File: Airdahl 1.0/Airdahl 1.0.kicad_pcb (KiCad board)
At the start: 2 copper layers, 60.5 x 38 mm, 94 parts, among them J1 Conn_01x04, J2 DF40C-34DS-0.4V_58_, J3 DF40C-34DS-0.4V_58_, J4 USB_C_Receptacle_USB2.0_16P, J7 CONUFL001-SMD-T, J9 104031-0811, SW1 SW_MEC_5E, SW2 SW_MEC_5E, U1 STM32F446RETx, U2 MCP2200-I-MQ, U4 BNO085, U5 BMP581, U6 RFM95W-915S2, U7 NCP1117-3.3_SOT223, Y1 ABM3B-8.000MHZ-12-D1X-T, Y2 ABS25-32.768KHZ-6-T, Y3 12MHz

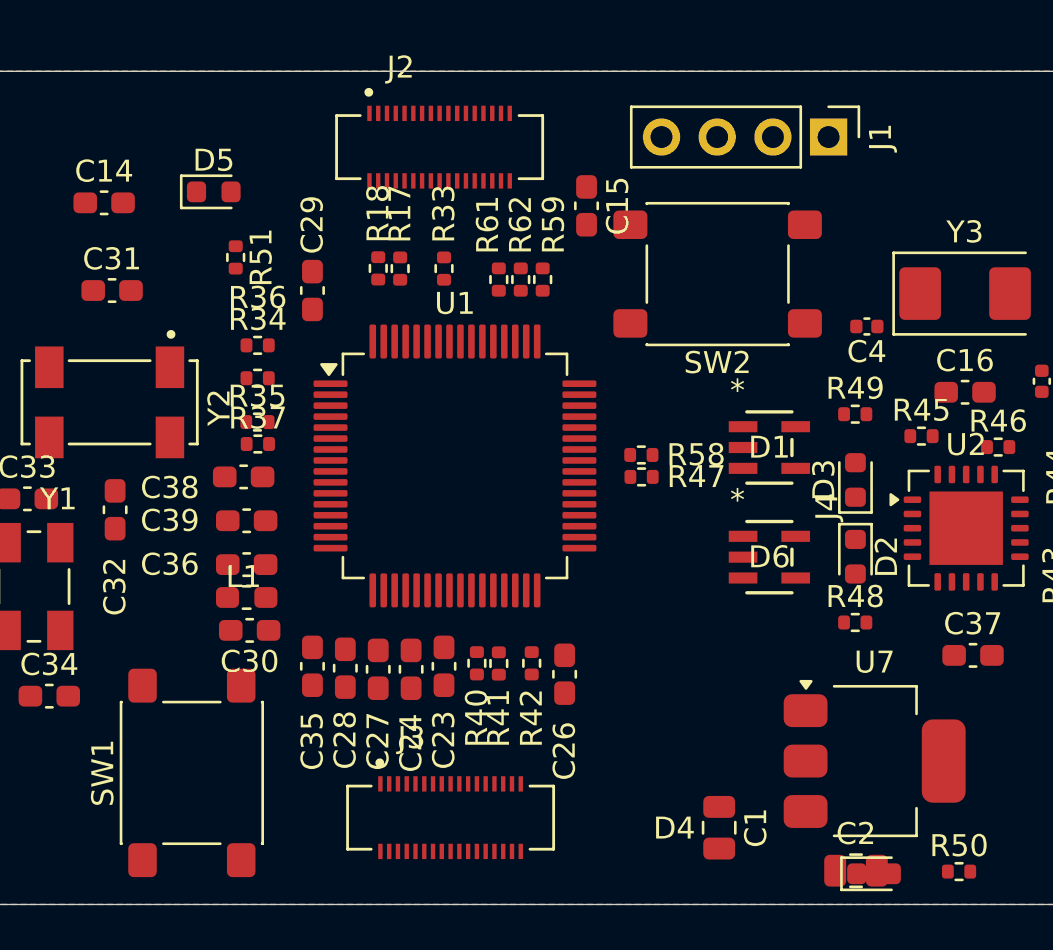
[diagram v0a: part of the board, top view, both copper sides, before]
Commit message: routed decoupling caps, might have to change in value.
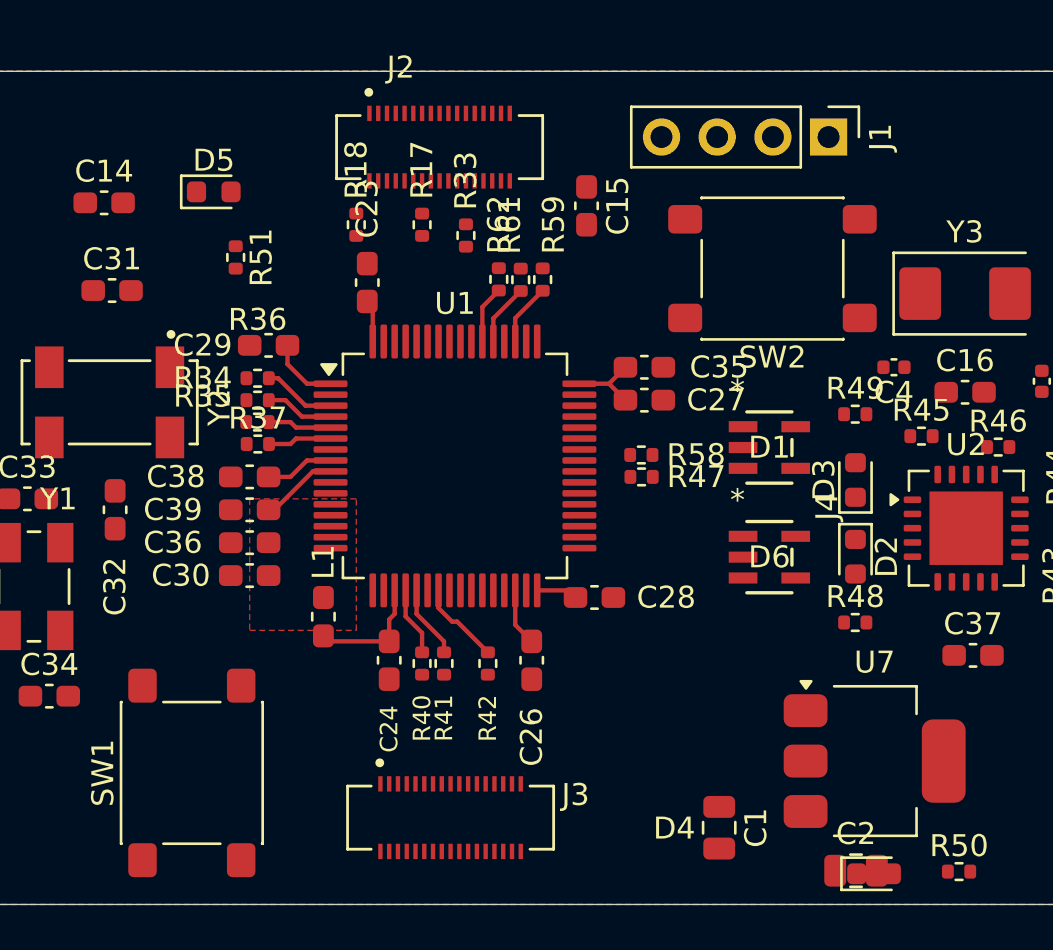
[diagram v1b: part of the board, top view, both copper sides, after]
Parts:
- moved C35 20.4 mm to (152.6, 69.0), turned to 0 degrees
- moved C23 17.8 mm to (140.0, 65.1), turned to 90 degrees
- moved C27 17.3 mm to (152.6, 70.5), turned to 0 degrees
- moved C28 11.8 mm to (150.4, 79.5), turned to 0 degrees
- moved L1 3.61 mm to (138.0, 80.4), turned to 90 degrees
- moved C29 3.20 mm to (135.5, 68.0), turned to 180 degrees
- moved SW2 2.51 mm to (158.5, 64.5)
- moved R40 2.50 mm to (142.5, 82.5)
- moved C30 2.50 mm to (134.6, 78.5)
- moved R41 2.50 mm to (143.5, 82.5)
- moved R17 2.24 mm to (142.5, 62.5)
- moved C4 2.23 mm to (164.0, 69.0)
- moved R18 2.23 mm to (139.5, 62.5)
- moved R42 2.00 mm to (145.5, 82.5)
- moved R33 1.81 mm to (144.5, 63.0)
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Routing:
- net +3V3: track 0.00 -> 12.8 mm
- net Net-(U1-PA7): track 0.00 -> 3.89 mm
- net /PAYLOAD_A: track 0.00 -> 3.55 mm
- net Net-(U1-PA5): track 0.00 -> 3.34 mm
- net Net-(U1-PC14): track 0.00 -> 3.33 mm
- net VBAT: track 0.00 -> 3.19 mm
- net Net-(U1-PA4): track 0.00 -> 3.14 mm
- net /PITOT_SGL: track 0.00 -> 3.14 mm
- net Net-(U1-PC15): track 0.00 -> 3.13 mm
- net Net-(U1-PH0): track 0.00 -> 2.93 mm
- net Net-(U1-PH1): track 0.00 -> 2.91 mm
- net Net-(U1-PC10): track 0.00 -> 2.83 mm
- net Net-(U1-PC12): track 0.00 -> 2.82 mm
- net Net-(U1-VCAP_1): track 0.00 -> 2.64 mm
- net Net-(U1-PD2): track 0.00 -> 2.64 mm
- added copper zone on F.Cu, net +3V3A

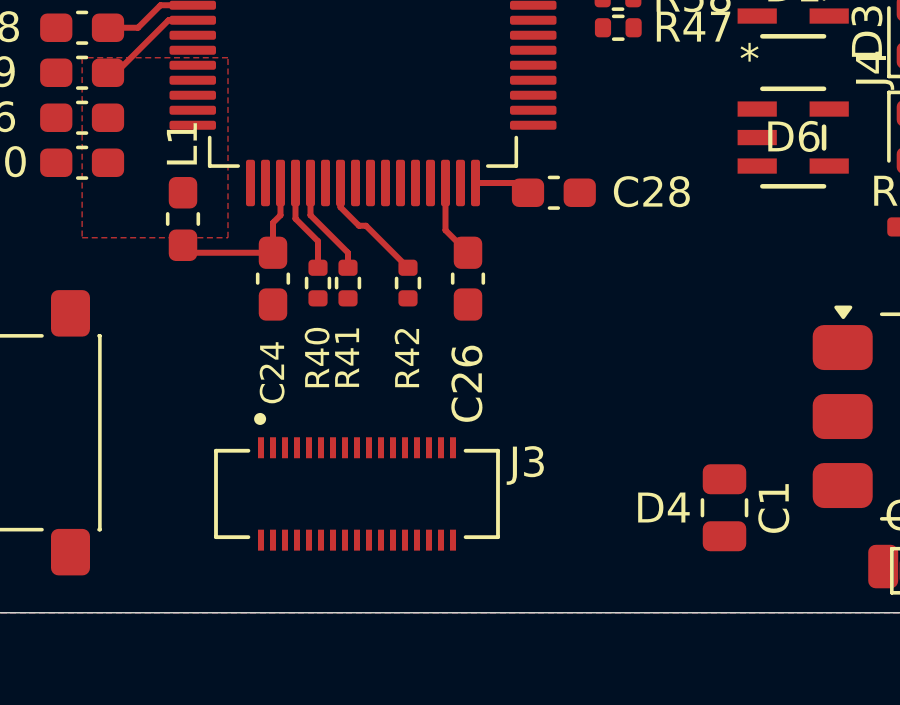
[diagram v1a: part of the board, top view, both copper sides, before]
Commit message: changed some of the connector pinouts, started some other routing
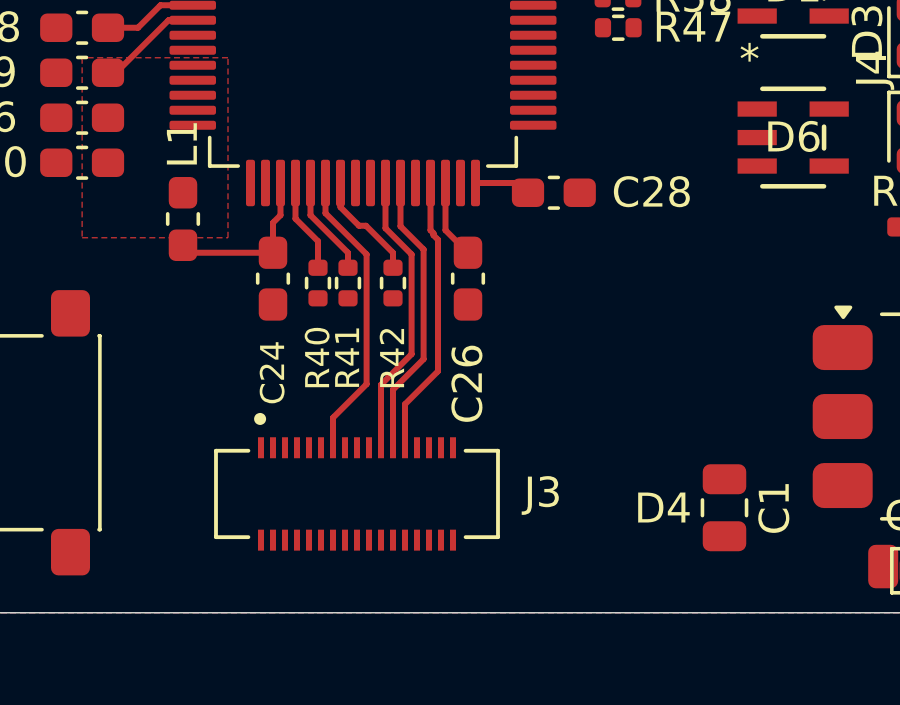
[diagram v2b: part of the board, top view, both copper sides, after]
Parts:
- moved R42 0.50 mm to (145.0, 82.5)
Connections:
- J2 pad 13: unconnected-(J2-Pad13) -> /PB3
- J2 pad 15: unconnected-(J2-Pad15) -> /PB4
- J2 pad 18: /PA3 -> unconnected-(J2-Pad18)
- J2 pad 19: unconnected-(J2-Pad19) -> /PB6
- J2 pad 21: unconnected-(J2-Pad21) -> /PAYLOAD_1F
- J2 pad 23: unconnected-(J2-Pad23) -> /PAYLOAD_1R
- J2 pad 28: /PYRO_4 -> unconnected-(J2-Pad28)
- J2 pad 29: /PAYLOAD_2R -> /SDA
- J2 pad 31: /PAYLOAD_2F -> /SCL
- J2 pad 33: /PC5 -> unconnected-(J2-Pad33)
- J3 pad 17: /PAYLOAD_1F -> /PA3
- J3 pad 19: /PAYLOAD_1R -> unconnected-(J3-Pad19)
- J3 pad 21: unconnected-(J3-Pad21) -> /PAYLOAD_2F
- J3 pad 23: unconnected-(J3-Pad23) -> /PAYLOAD_2R
- J3 pad 25: unconnected-(J3-Pad25) -> /PYRO_4
- J3 pad 27: /SDA -> /PC5
- J3 pad 28: /PB6 -> unconnected-(J3-Pad28)
- J3 pad 29: /SCL -> unconnected-(J3-Pad29)
- J3 pad 32: /PB4 -> unconnected-(J3-Pad32)
- J3 pad 34: /PB3 -> unconnected-(J3-Pad34)
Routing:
- net /MISO: track 0.00 -> 9.86 mm
- net /PAYLOAD_2F: track 0.00 -> 9.61 mm
- net /PAYLOAD_2R: track 0.00 -> 9.57 mm
- net /PYRO_4: track 0.00 -> 9.38 mm
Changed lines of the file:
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@@
 			(size 0.2 0.7)
 			(layers "F.Cu" "F.Mask")
-			(net "unconnected-(J2-Pad13)")
+			(net "/PB3")
 			(pinfunction "13_13")
 			(pintype "passive")
@@
 			(size 0.2 0.7)
 			(layers "F.Cu" "F.Mask")
-			(net "unconnected-(J2-Pad15)")
+			(net "/PB4")
 			(pinfunction "15_15")
 			(pintype "passive")
@@
 			(size 0.2 0.7)
 			(layers "F.Cu" "F.Mask")
-			(net "/PA3")
+			(net "unconnected-(J2-Pad18)")
 			(pinfunction "18_18")
 			(pintype "passive")
@@
 			(size 0.2 0.7)
 			(layers "F.Cu" "F.Mask")
-			(net "unconnected-(J2-Pad19)")
+			(net "/PB6")
 			(pinfunction "19_19")
 			(pintype "passive")
@@
 			(size 0.2 0.7)
 			(layers "F.Cu" "F.Mask")
-			(net "unconnected-(J2-Pad21)")
+			(net "/PAYLOAD_1F")
 			(pinfunction "21_21")
 			(pintype "passive")
@@
 			(size 0.2 0.7)
 			(layers "F.Cu" "F.Mask")
-			(net "unconnected-(J2-Pad23)")
+			(net "/PAYLOAD_1R")
 			(pinfunction "23_23")
 			(pintype "passive")
@@
 			(size 0.2 0.7)
 			(layers "F.Cu" "F.Mask")
-			(net "/PYRO_4")
+			(net "unconnected-(J2-Pad28)")
 			(pinfunction "28_28")
 			(pintype "passive")
@@
 			(size 0.2 0.7)
 			(layers "F.Cu" "F.Mask")
-			(net "/PAYLOAD_2R")
+			(net "/SDA")
 			(pinfunction "29_29")
 			(pintype "passive")
@@
 			(size 0.2 0.7)
 			(layers "F.Cu" "F.Mask")
-			(net "/PAYLOAD_2F")
+			(net "/SCL")
 			(pinfunction "31_31")
 			(pintype "passive")
@@
 			(size 0.2 0.7)
 			(layers "F.Cu" "F.Mask")
-			(net "/PC5")
+			(net "unconnected-(J2-Pad33)")
 			(pinfunction "33_33")
 			(pintype "passive")
@@
 		(at 143.8 89.54)
 		(property "Reference" "J3"
-			(at 5.7 -1.04 0)
+			(at 6.2 -0.04 0)
 			(layer "F.SilkS")
 			(effects
@@
 			(size 0.2 0.7)
 			(layers "F.Cu" "F.Mask")
-			(net "/PAYLOAD_1F")
+			(net "/PA3")
 			(pinfunction "17_17")
 			(pintype "passive")
@@
 			(size 0.2 0.7)
 			(layers "F.Cu" "F.Mask")
-			(net "/PAYLOAD_1R")
+			(net "unconnected-(J3-Pad19)")
 			(pinfunction "19_19")
 			(pintype "passive")
@@
 			(size 0.2 0.7)
 			(layers "F.Cu" "F.Mask")
-			(net "unconnected-(J3-Pad21)")
+			(net "/PAYLOAD_2F")
 			(pinfunction "21_21")
 			(pintype "passive")
@@
 			(size 0.2 0.7)
 			(layers "F.Cu" "F.Mask")
-			(net "unconnected-(J3-Pad23)")
+			(net "/PAYLOAD_2R")
 			(pinfunction "23_23")
 			(pintype "passive")
@@
 			(size 0.2 0.7)
 			(layers "F.Cu" "F.Mask")
-			(net "unconnected-(J3-Pad25)")
+			(net "/PYRO_4")
 			(pinfunction "25_25")
 			(pintype "passive")
@@
 			(size 0.2 0.7)
 			(layers "F.Cu" "F.Mask")
-			(net "/SDA")
+			(net "/PC5")
 			(pinfunction "27_27")
 			(pintype "passive")
@@
 			(size 0.2 0.7)
 			(layers "F.Cu" "F.Mask")
-			(net "/PB6")
+			(net "unconnected-(J3-Pad28)")
 			(pinfunction "28_28")
 			(pintype "passive")
@@
 			(size 0.2 0.7)
 			(layers "F.Cu" "F.Mask")
-			(net "/SCL")
+			(net "unconnected-(J3-Pad29)")
 			(pinfunction "29_29")
 			(pintype "passive")
@@
 			(size 0.2 0.7)
 			(layers "F.Cu" "F.Mask")
-			(net "/PB4")
+			(net "unconnected-(J3-Pad32)")
 			(pinfunction "32_32")
 			(pintype "passive")
@@
 			(size 0.2 0.7)
 			(layers "F.Cu" "F.Mask")
-			(net "/PB3")
+			(net "unconnected-(J3-Pad34)")
 			(pinfunction "34_34")
 			(pintype "passive")
@@
 	(footprint "Resistor_SMD:R_0402_1005Metric"
 		(layer "F.Cu")
-		(at 145.5 82.51 90)
+		(at 145 82.51 90)
 		(descr "Resistor SMD 0402 (1005 Metric), square (rectangular) end terminal, IPC-7351 nominal, (Body size source: IPC-SM-782 page 72, https://www.pcb-3d.com/wordpress/wp-content/uploads/ipc-sm-782a_amendment_1_and_2.pdf)")
 		(tags "resistor")
@@
 	)
 	(segment
-		(start 143.25 79.98241)
-		(end 143.86759 80.6)
+		(start 142.75 79.175)
+		(end 142.75 80.184314)
 		(width 0.2)
 		(layer "F.Cu")
-		(net "Net-(U1-PA7)")
+		(net "/MISO")
 	)
 	(segment
-		(start 143.86759 80.6)
-		(end 144.1 80.6)
+		(start 143 87)
+		(end 143 88)
+		(width 0.2)
+		(layer "F.Cu")
+		(net "/MISO")
+	)
+	(segment
+		(start 144.12 81.554314)
+		(end 144.12 85.88)
+		(width 0.2)
+		(layer "F.Cu")
+		(net "/MISO")
+	)
+	(segment
+		(start 142.75 80.184314)
+		(end 144.12 81.554314)
+		(width 0.2)
+		(layer "F.Cu")
+		(net "/MISO")
+	)
+	(segment
+		(start 144.12 85.88)
+		(end 143 87)
+		(width 0.2)
+		(layer "F.Cu")
+		(net "/MISO")
+	)
+	(segment
+		(start 145 81.5)
+		(end 145 82)
 		(width 0.2)
 		(layer "F.Cu")
@@
 	(segment
 		(start 144.1 80.6)
-		(end 145.5 82)
+		(end 145 81.5)
+		(width 0.2)
+		(layer "F.Cu")
+		(net "Net-(U1-PA7)")
+	)
+	(segment
+		(start 143.86759 80.6)
+		(end 144.1 80.6)
+		(width 0.2)
+		(layer "F.Cu")
+		(net "Net-(U1-PA7)")
+	)
+	(segment
+		(start 143.25 79.98241)
+		(end 143.86759 80.6)
 		(width 0.2)
 		(layer "F.Cu")
@@
 	)
 	(segment
+		(start 145.62 84.88)
+		(end 144.6 85.9)
+		(width 0.2)
+		(layer "F.Cu")
+		(net "/PAYLOAD_2F")
+	)
+	(segment
+		(start 144.75 80.684314)
+		(end 145.62 81.554314)
+		(width 0.2)
+		(layer "F.Cu")
+		(net "/PAYLOAD_2F")
+	)
+	(segment
+		(start 145.62 81.554314)
+		(end 145.62 84.88)
+		(width 0.2)
+		(layer "F.Cu")
+		(net "/PAYLOAD_2F")
+	)
+	(segment
+		(start 144.75 79.175)
+		(end 144.75 80.684314)
+		(width 0.2)
+		(layer "F.Cu")
+		(net "/PAYLOAD_2F")
+	)
+	(segment
+		(start 144.6 85.9)
+		(end 144.6 88)
+		(width 0.2)
+		(layer "F.Cu")
+		(net "/PAYLOAD_2F")
+	)
+	(segment
+		(start 145.25 80.618628)
+		(end 146.02 81.388628)
+		(width 0.2)
+		(layer "F.Cu")
+		(net "/PAYLOAD_2R")
+	)
+	(segment
+		(start 146.02 81.388628)
+		(end 146.02 85.045686)
+		(width 0.2)
+		(layer "F.Cu")
+		(net "/PAYLOAD_2R")
+	)
+	(segment
+		(start 145 86.065686)
+		(end 145 88)
+		(width 0.2)
+		(layer "F.Cu")
+		(net "/PAYLOAD_2R")
+	)
+	(segment
+		(start 145.25 79.175)
+		(end 145.25 80.618628)
+		(width 0.2)
+		(layer "F.Cu")
+		(net "/PAYLOAD_2R")
+	)
+	(segment
+		(start 146.02 85.045686)
+		(end 145 86.065686)
+		(width 0.2)
+		(layer "F.Cu")
+		(net "/PAYLOAD_2R")
+	)
+	(segment
+		(start 145.4 86.55)
+		(end 145.4 88)
+		(width 0.2)
+		(layer "F.Cu")
+		(net "/PYRO_4")
+	)
+	(segment
+		(start 146.25 80.75)
+		(end 146.35 80.85)
+		(width 0.2)
+		(layer "F.Cu")
+		(net "/PYRO_4")
+	)
+	(segment
+		(start 146.5 81.065685)
+		(end 146.5 85.45)
+		(width 0.2)
+		(layer "F.Cu")
+		(net "/PYRO_4")
+	)
+	(segment
+		(start 146.35 80.85)
+		(end 146.35 80.915686)
+		(width 0.2)
+		(layer "F.Cu")
+		(net "/PYRO_4")
+	)
+	(segment
+		(start 146.25 79.175)
+		(end 146.25 80.75)
+		(width 0.2)
+		(layer "F.Cu")
+		(net "/PYRO_4")
+	)
+	(segment
+		(start 146.35 80.915686)
+		(end 146.5 81.065685)
+		(width 0.2)
+		(layer "F.Cu")
+		(net "/PYRO_4")
+	)
+	(segment
+		(start 146.5 85.45)
+		(end 145.4 86.55)
+		(width 0.2)
+		(layer "F.Cu")
+		(net "/PYRO_4")
+	)
+	(segment

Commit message: the diff pairs are eating my lunch
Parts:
- SW1, SW2: value SW_MEC_5E -> SW_SPST
- moved BT1 154.2 mm to (113.0, 126.3), turned to -90 degrees
- moved R26 128.6 mm to (120.8, 174.9)
- moved C10 128.6 mm to (136.8, 158.5)
- moved C12 128.6 mm to (138.8, 165.5)
- moved C13 128.6 mm to (146.6, 149.0)
- moved C17 128.6 mm to (147.8, 144.5)
- moved C6 128.6 mm to (121.9, 155.8)
- moved C7 128.6 mm to (118.9, 160.3)
- moved J9 128.6 mm to (141.6, 173.3)
- moved R19 128.6 mm to (125.2, 172.3)
- moved R20 128.6 mm to (125.2, 174.9)
- moved R21 128.6 mm to (125.6, 169.3)
- moved R22 128.6 mm to (121.2, 165.8)
- moved R24 128.6 mm to (129.8, 160.3)
- moved R25 128.6 mm to (120.8, 172.3)
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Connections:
- net /USB_DM renamed /USB_D_N
- net /USB_DP renamed /USB_D_P
- J2 pad 10: /PC3 -> /SCL
- J2 pad 12: /PA0 -> /PAYLOAD_1R
- J2 pad 14: /PA1 -> /PAYLOAD_1F
- J2 pad 21: /PAYLOAD_1F -> /PC2
- J2 pad 23: /PAYLOAD_1R -> unconnected-(J2-Pad23)
- J2 pad 29: /SDA -> /PA1
- J2 pad 31: /SCL -> /PA0
- J2 pad 33: unconnected-(J2-Pad33) -> /PC3
- J2 pad 8: /PC2 -> /SDA
- SW1 pad 1: /NRST -> GND
- SW2 pad 1: +3V3 -> /BOOT0
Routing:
- net /USB_D_N: track 0.00 -> 15.1 mm, vias 0 -> 2
- net /USB_D_P: track 0.00 -> 14.6 mm, vias 0 -> 2
- net Net-(U2-OSC1): track 0.00 -> 10.3 mm
- net Net-(U2-OSC2): track 0.00 -> 10.0 mm
- net /NRST: track 0.00 -> 9.52 mm, vias 0 -> 1
- net /PAYLOAD_1R: track 0.00 -> 8.01 mm
- net /SDA: track 0.00 -> 7.35 mm
- net /SCL: track 0.00 -> 7.35 mm
- net /UART_RX: track 0.00 -> 7.18 mm, vias 0 -> 2
- net Net-(C31-Pad2): track 0.00 -> 6.90 mm
- net Net-(C32-Pad2): track 0.00 -> 6.69 mm
- net USB_3V3: track 0.00 -> 5.87 mm
- net VBUS: track 0.00 -> 5.76 mm
- net /MOSI: track 0.00 -> 5.64 mm
- net /UART_TX: track 0.00 -> 5.61 mm
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- added copper zone on F.Cu, net VBUS
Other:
- board size 60.5 x 38 mm -> 57.6 x 38.5 mm

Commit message: routing changes
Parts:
- C10, C12, C5, C6, C7, R19, R20, R21, R22, R24, R25, R26, R27, U4, U5: moved to F.Cu
- C37: value 100n -> 330n
- moved R26 102.0 mm to (161.2, 81.2), turned to -90 degrees
- moved R25 99.2 mm to (164.5, 83.2), turned to -90 degrees
- moved R20 92.6 mm to (153.6, 86.8), turned to 0 degrees
- moved J9 90.3 mm to (211.1, 115.7), turned to 90 degrees
- moved R19 89.2 mm to (161.0, 90.7), turned to 90 degrees
- moved C12 89.0 mm to (173.2, 83.5), turned to 90 degrees
- moved R22 87.3 mm to (164.3, 90.0), turned to 180 degrees
- moved R27 84.3 mm to (174.2, 89.2), turned to 0 degrees
- moved R21 83.5 mm to (153.2, 90.6), turned to -90 degrees
- moved C7 83.0 mm to (153.6, 85.0)
- moved U5 82.9 mm to (172.5, 86.8), turned to 0 degrees
- moved C10 82.6 mm to (175.0, 85.2), turned to 90 degrees
- moved C6 82.1 mm to (157.2, 81.8), turned to 90 degrees
- moved U4 82.0 mm to (159.0, 85.9), turned to 0 degrees
- moved C5 80.7 mm to (157.8, 90.0), turned to -90 degrees
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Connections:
- J2 pad 12: /PAYLOAD_1R -> unconnected-(J2-Pad12)
- J2 pad 14: /PAYLOAD_1F -> /PAYLOAD_1R
- J2 pad 16: /PA2 -> /PAYLOAD_1F
- J2 pad 20: /PYRO_5 -> /PC5
- J2 pad 22: /PYRO_1 -> unconnected-(J2-Pad22)
- J2 pad 24: /PYRO_2 -> unconnected-(J2-Pad24)
- J2 pad 26: /PYRO_3 -> unconnected-(J2-Pad26)
- J2 pad 29: /PA1 -> unconnected-(J2-Pad29)
- J2 pad 31: /PA0 -> unconnected-(J2-Pad31)
- J3 pad 12: unconnected-(J3-Pad12) -> +3V3_REG
- J3 pad 17: /PA3 -> /UART_RX
- J3 pad 19: unconnected-(J3-Pad19) -> /UART_TX
- J3 pad 25: /PYRO_4 -> /PYRO_5
- J3 pad 27: /PC5 -> /PYRO_4
- J3 pad 29: unconnected-(J3-Pad29) -> /PYRO_3
- J3 pad 3: /UART_RX -> unconnected-(J3-Pad3)
- J3 pad 31: GND -> /PYRO_2
- J3 pad 32: unconnected-(J3-Pad32) -> GND
- J3 pad 33: GND -> /PYRO_1
- J3 pad 34: unconnected-(J3-Pad34) -> GND
- J3 pad 4: unconnected-(J3-Pad4) -> /PA0
- J3 pad 5: /UART_TX -> /PA3
- J3 pad 6: unconnected-(J3-Pad6) -> /PA1
- J3 pad 8: +3V3_REG -> /PA2
- U1 pad 29: /PYRO_4 -> /PYRO_5
- U1 pad 33: /PYRO_3 -> /PYRO_4
- U1 pad 34: /PYRO_2 -> /PYRO_3
- U1 pad 35: /PYRO_1 -> /PYRO_2
- U1 pad 36: /PYRO_5 -> /PYRO_1
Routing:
- net GND: track 0.00 -> 50.2 mm, vias 0 -> 38
- net /PAYLOAD_1F: track 0.00 -> 20.2 mm, vias 0 -> 2
- net /PWM: track 0.00 -> 18.8 mm, vias 0 -> 2
- net /PYRO_1: track 0.00 -> 18.5 mm, vias 0 -> 2
- net /SWDIO: track 0.00 -> 17.7 mm, vias 0 -> 1
- net /PYRO_2: track 0.00 -> 17.5 mm, vias 0 -> 2
- net /SDA: track 7.35 -> 24.3 mm, vias 0 -> 3
- net /PYRO_3: track 0.00 -> 16.4 mm, vias 0 -> 2
- net Net-(D3-K): track 0.00 -> 14.9 mm, vias 0 -> 2
- net Net-(D2-K): track 0.00 -> 14.5 mm, vias 0 -> 2
- net /SCL: track 7.35 -> 20.2 mm, vias 0 -> 1
- net /SWCLK: track 0.00 -> 12.0 mm, vias 0 -> 1
- net +3V3: track 14.6 -> 25.9 mm
- net Net-(C33-Pad2): track 0.00 -> 10.5 mm
- net /PYRO_5: track 0.00 -> 9.38 mm
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- added copper zone on F.Cu, net GND
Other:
- board size 57.6 x 38.5 mm -> 57.6 x 39.5 mm
